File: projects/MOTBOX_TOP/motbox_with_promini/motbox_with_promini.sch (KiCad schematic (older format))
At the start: 28 parts, among them J1 12V IN, J2 Manual EN, J3 OBS_IR_TX, J4 OP_CL_OBS_DET_LED, J5 OBS IR RX, J6 Open Close Done, J7 Motor, P1 Digital, P2 ADC, P3 COM, P4 ADC, P5 Analog, U1 LM2575-5.0BU, U2 LM393, U3 L293D

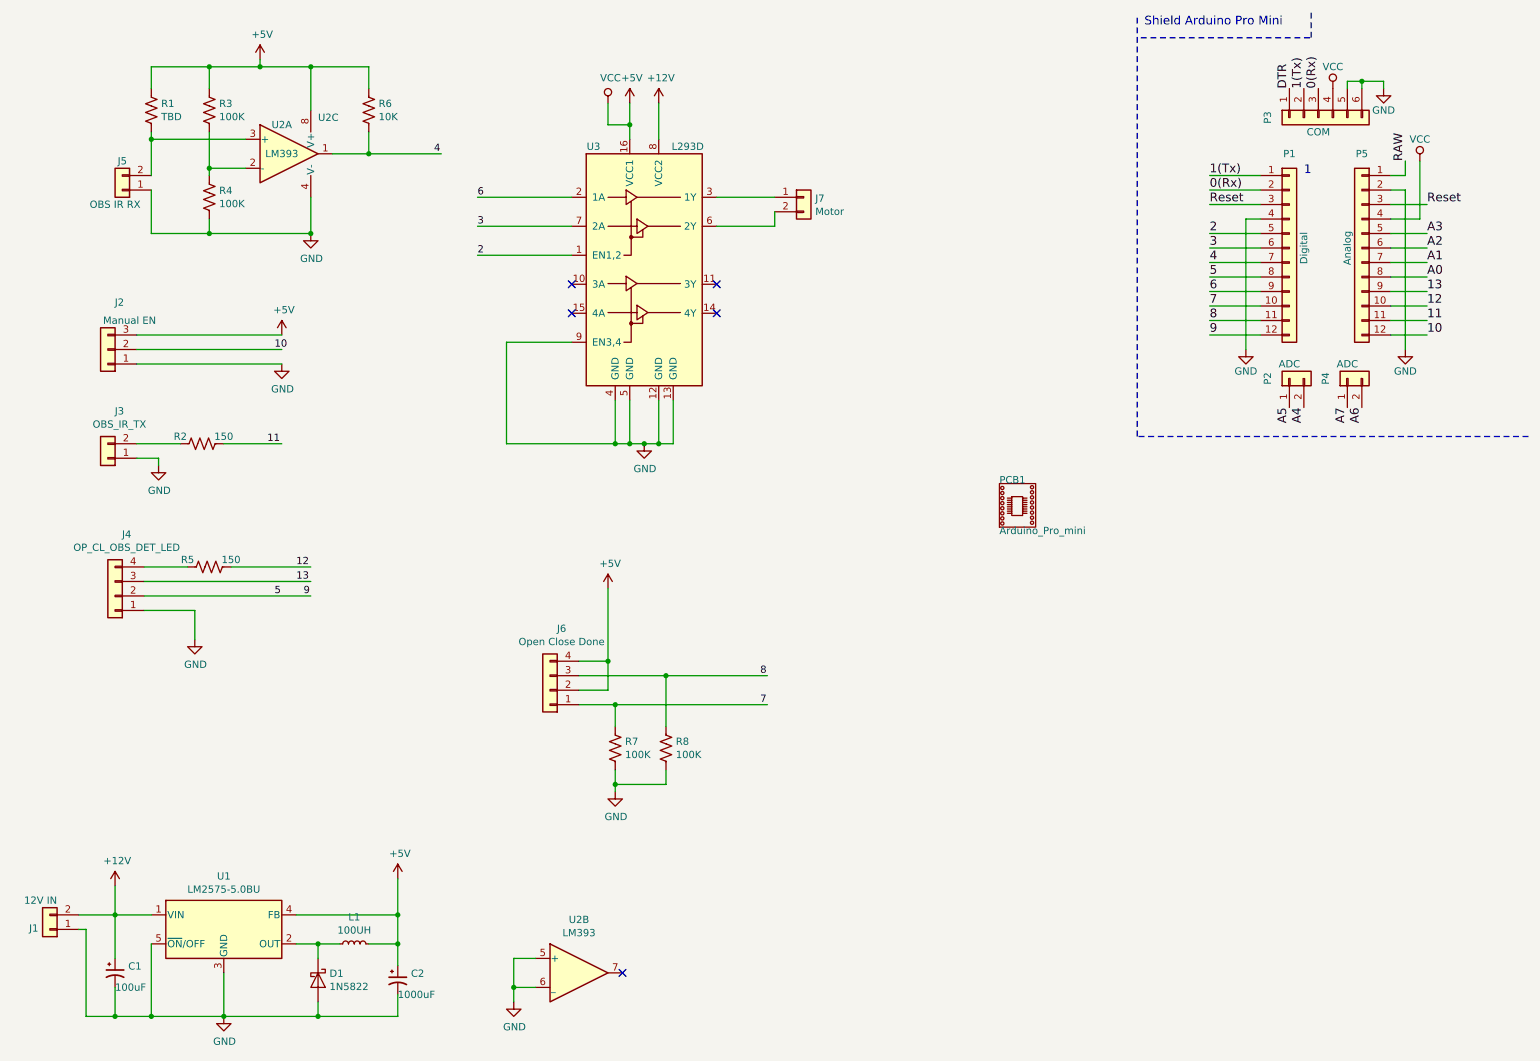
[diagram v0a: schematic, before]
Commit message: New library files and schematics with ESE31 and DT045 switches
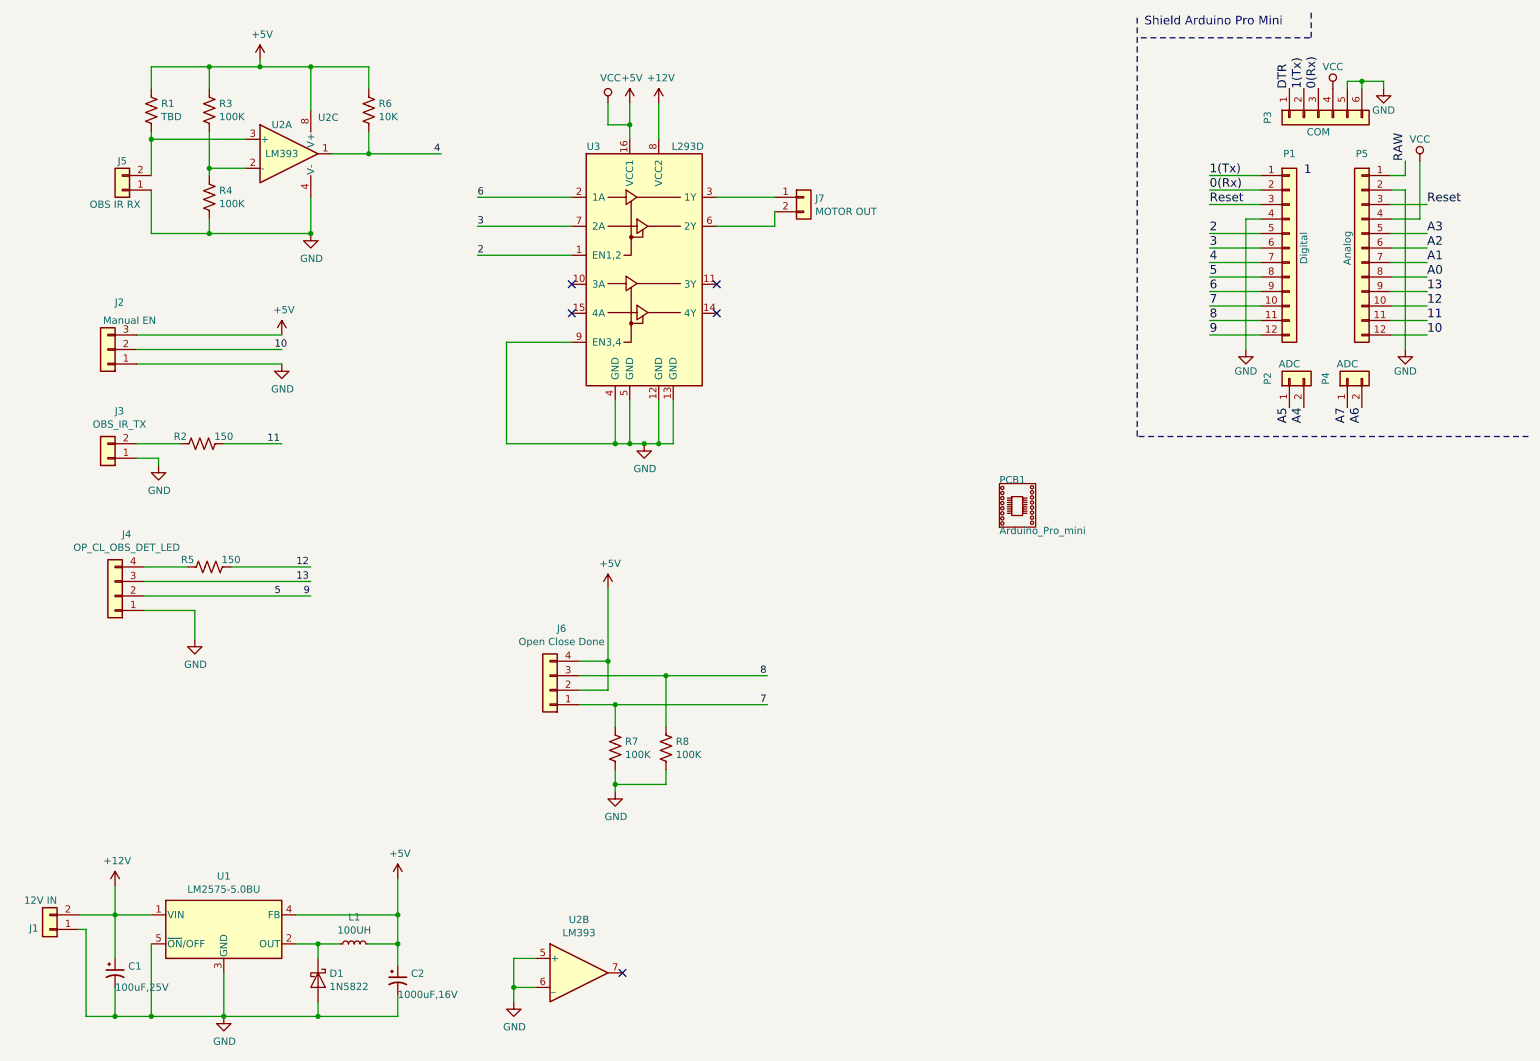
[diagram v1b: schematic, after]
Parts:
- C1: value 100uF -> 100uF,25V
- C2: value 1000uF -> 1000uF,16V
- J7: value Motor -> MOTOR OUT
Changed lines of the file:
@@
 AR Path="/5CC2F2FF" Ref="J7"  Part="1"
 F 0 "J7" H 6280 1792 50  0000 L CNN
-F 1 "Motor" H 6280 1701 50  0000 L CNN
+F 1 "MOTOR OUT" H 6280 1701 50  0000 L CNN
 F 2 "Connector_JST:JST_EH_B02B-EH-A_1x02_P2.50mm_Vertical" H 6200 1800 50  0001 C CNN
 F 3 "~" H 6200 1800 50  0001 C CNN
@@
 AR Path="/5CC2F314" Ref="C1"  Part="1"
 F 0 "C1" H 1541 7196 50  0000 L CNN
-F 1 "100uF" H 1450 7050 50  0000 L CNN
+F 1 "100uF,25V" H 1450 7050 50  0000 L CNN
 F 2 "Capacitor_SMD:CP_Elec_6.3x7.7" H 1450 7150 50  0001 C CNN
 F 3 "~" H 1450 7150 50  0001 C CNN
@@
 AR Path="/5CC2F31B" Ref="C2"  Part="1"
 F 0 "C2" H 3491 7246 50  0000 L CNN
-F 1 "1000uF" H 3400 7100 50  0000 L CNN
+F 1 "1000uF,16V" H 3400 7100 50  0000 L CNN
 F 2 "Capacitor_SMD:CP_Elec_10x10" H 3400 7200 50  0001 C CNN
 F 3 "~" H 3400 7200 50  0001 C CNN
